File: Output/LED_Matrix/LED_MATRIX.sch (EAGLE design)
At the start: 36 parts

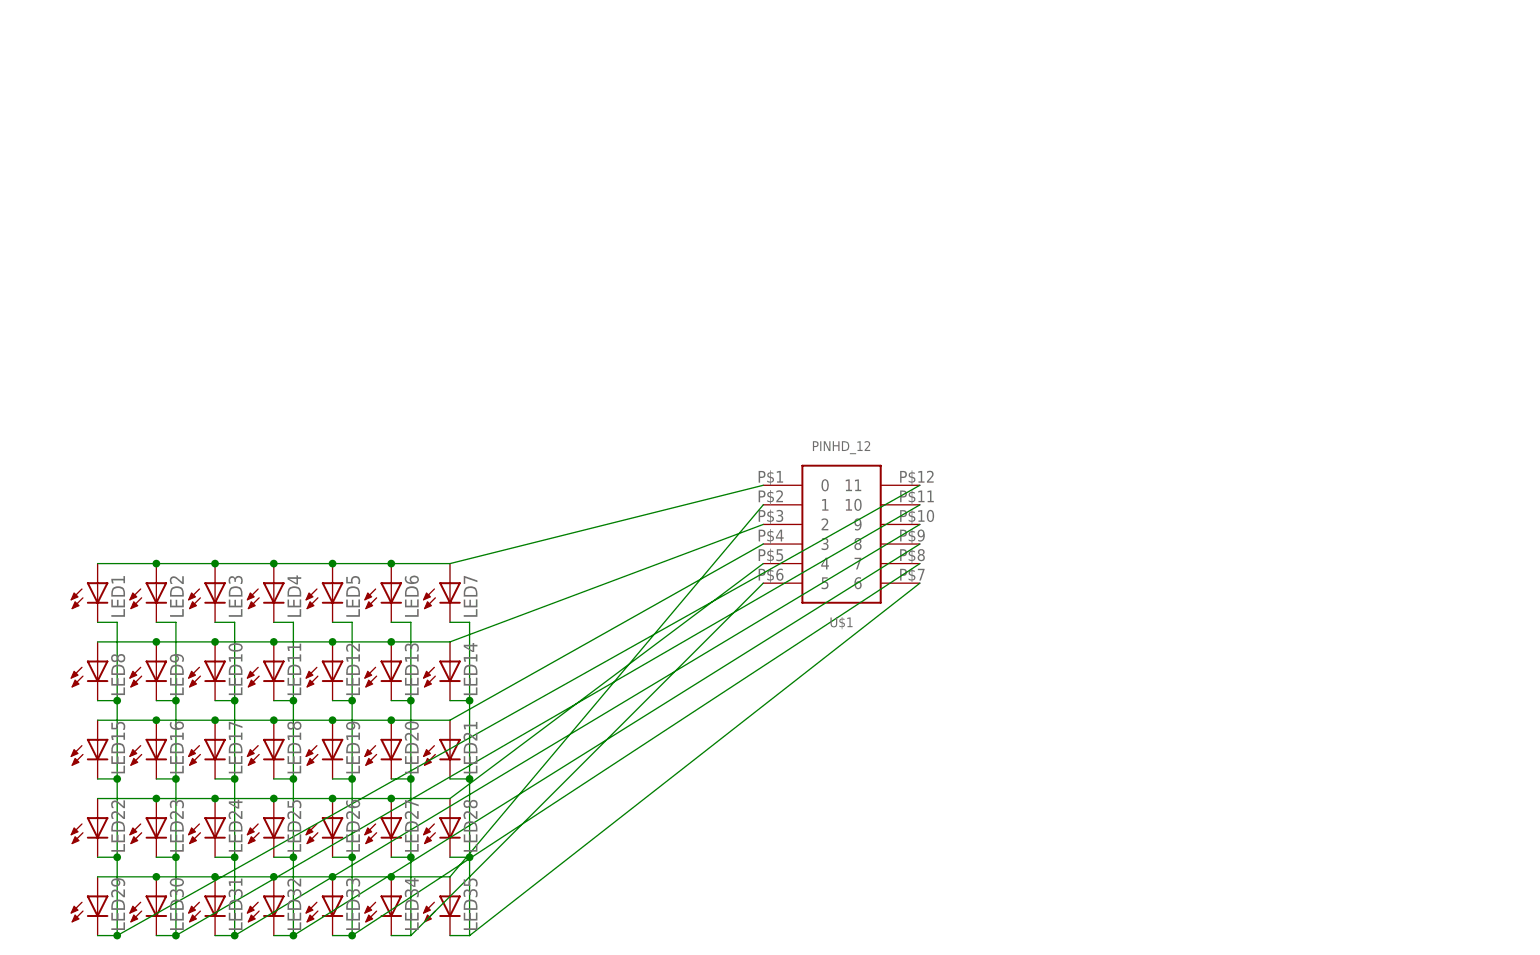
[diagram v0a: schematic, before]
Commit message: Update Pinheader
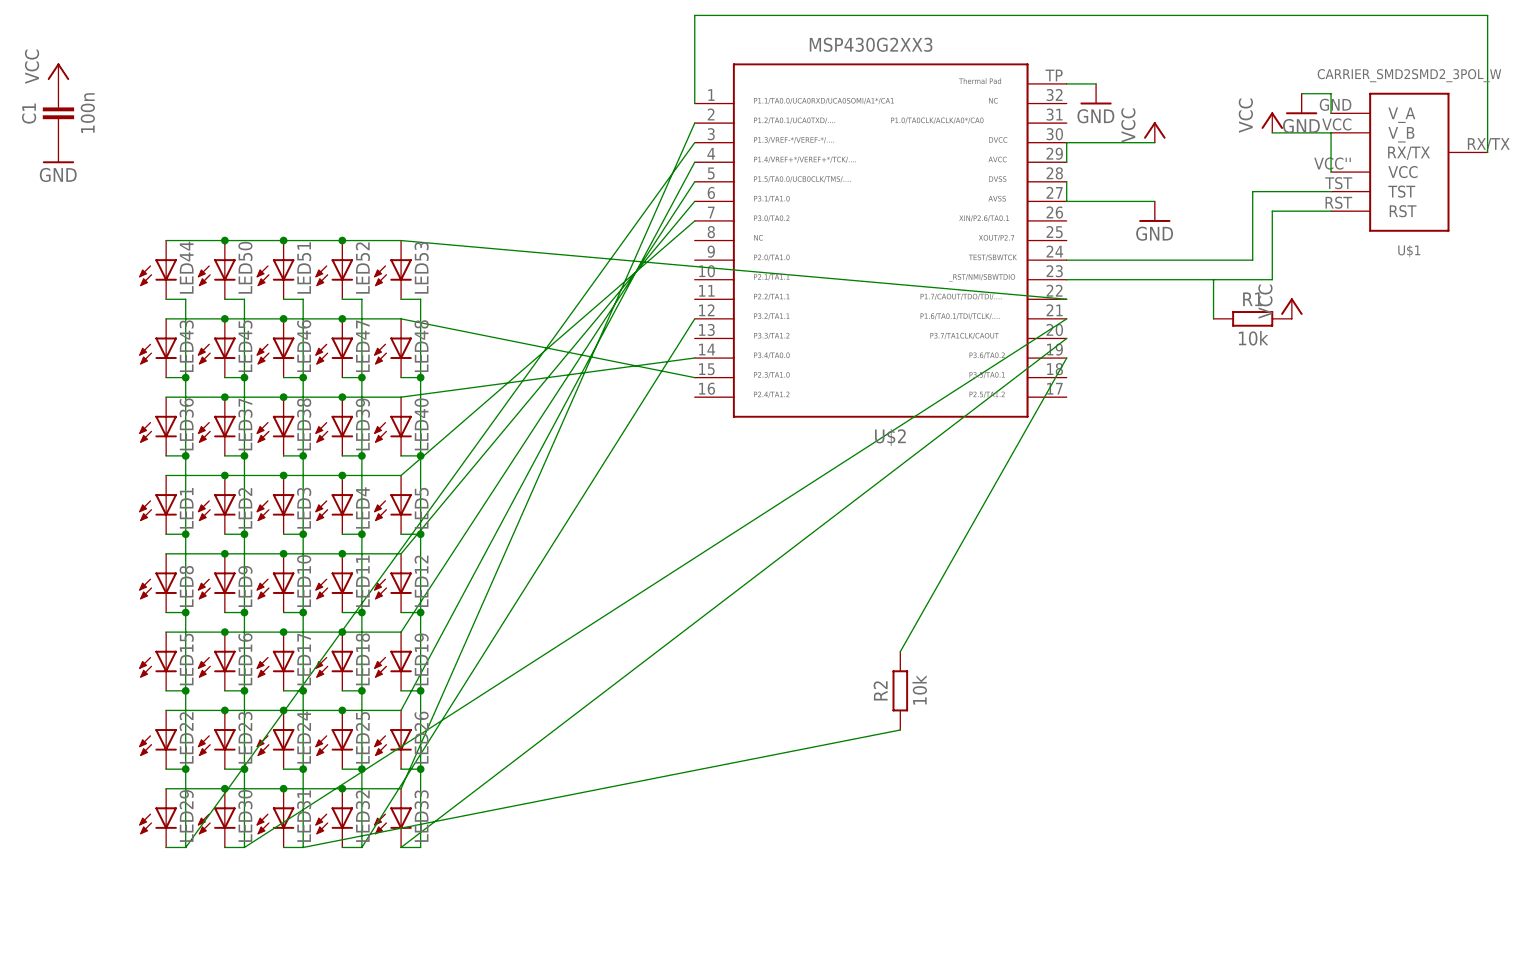
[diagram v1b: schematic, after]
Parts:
- removed LED13, LED14, LED20, LED21, LED27, LED28, LED34, LED35, LED6, LED7: (no value), led:LEDCHIPLED_0603
- added C1: 100n, thar:CAPACITOR
- added LED36, LED37, LED38, LED39, LED40, LED43, LED44, LED45, LED46, LED47, LED48, LED50, LED51, LED52, LED53: (no value), led:LEDCHIPLED_0603
- added R1: 10k, thar:RESISTOR0603
- added R2: 10k, thar:RESISTOR0603S
- added U$2: MSP430G2553, thar:MSP430G2553
- U$1: value PINHD_12 -> CARRIER_SMD2SMD2_3POL_W; device thar:PINHD_12 -> thar:CARRIER_SMD2SMD2_3POL_W
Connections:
- removed net N$48: LED13.C, LED20.C, LED27.C, LED34.C, LED6.C, U$1.5
- removed net N$49: LED14.C, LED21.C, LED28.C, LED35.C, LED7.C, U$1.6
- new net GND: C1.1, U$1.V_A, U$2.27, U$2.28, U$2.TP
- new net N$12: U$1.RX/TX, U$2.1
- new net N$2: U$1.TST, U$2.24
- new net N$20: LED36.A, LED37.A, LED38.A, LED39.A, LED40.A, U$2.14
- new net N$21: LED44.A, LED50.A, LED51.A, LED52.A, LED53.A, U$2.22
- new net N$23: LED43.A, LED45.A, LED46.A, LED47.A, LED48.A, U$2.15
- new net N$25: R2.2, U$2.19
- new net N$4: R1.1, U$1.RST, U$2.23
- new net VCC: C1.2, R1.2, U$1.VCC, U$1.V_B, U$2.29, U$2.30
- net N$38: now also U$2.7; no longer LED6.A, LED7.A, U$1.0
- net N$39: now also U$2.6; no longer LED13.A, LED14.A, U$1.2
- net N$40: now also U$2.5; no longer LED20.A, LED21.A, U$1.3
- net N$41: now also U$2.4; no longer LED27.A, LED28.A, U$1.4
- net N$42: now also U$2.2; no longer LED34.A, LED35.A, U$1.1
- net N$43: now also LED36.C, LED43.C, LED44.C, U$2.3; no longer U$1.11
- net N$44: now also LED37.C, LED45.C, LED50.C, U$2.21; no longer U$1.10
- net N$45: now also LED38.C, LED46.C, LED51.C, R2.1; no longer U$1.9
- net N$46: now also LED39.C, LED47.C, LED52.C, U$2.12; no longer U$1.8
- net N$47: now also LED40.C, LED48.C, LED53.C, U$2.20; no longer U$1.7
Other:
- moved on the sheet: LED1, LED10, LED11, LED12, LED15, LED16, LED17, LED18, LED19, LED2, LED22, LED23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
